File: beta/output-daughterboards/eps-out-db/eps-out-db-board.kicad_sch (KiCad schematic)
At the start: 7 parts, among them J1 EPS8 OUT FIELD, J10 TE 63951-1, J11 TE 63951-1, J12 TE 63951-1, J13 TE 63951-1, J14 TE 63951-1, J15 TE 63951-1

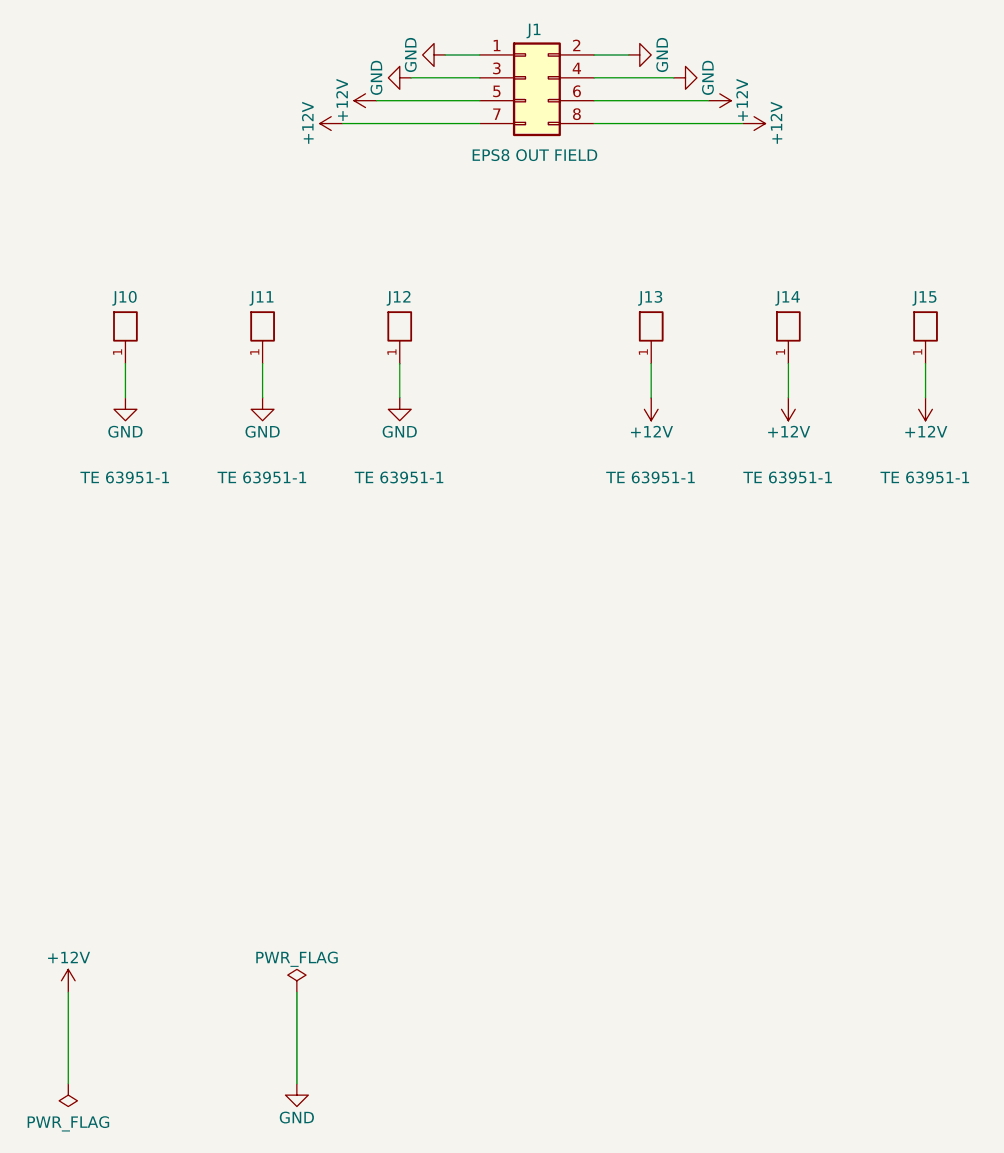
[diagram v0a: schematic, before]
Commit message: pipeline: integrate route-aware physical design flow
Generalize critical-first placement and routing, future-congestion and power-authority planning, route provenance, process watchdogs, fab/thermal validation, dashboard review, and XFCN integration. Add the supporting board contracts, component libraries, documentation, and regression coverage.
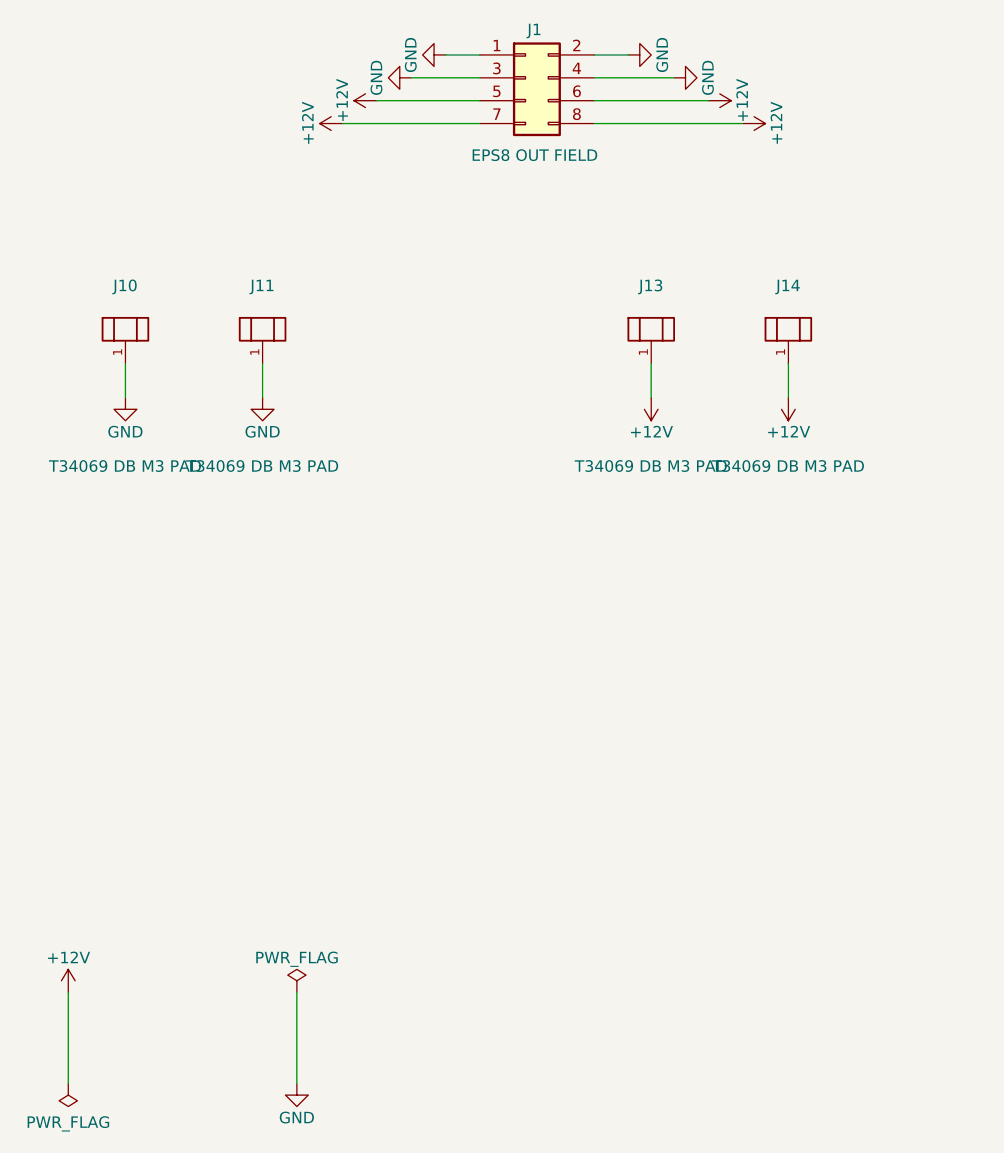
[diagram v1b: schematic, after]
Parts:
- removed J12, J15: TE 63951-1, cec-Connector_Blade:TE_63951-1_FASTON_Tab_250x032_RA_THT, symbol cec-vendor:TE_63951-1_FASTON_Tab
- J10, J11, J13, J14: value TE 63951-1 -> T34069 DB M3 PAD; footprint cec-Connector_Blade:TE_63951-1_FASTON_Tab_250x032_RA_THT -> cec-Connector_Screw:XFCN_T34069_Daughterboard_BoltPad_M3_PROVISIONAL; symbol cec-vendor:TE_63951-1_FASTON_Tab -> cec-Connector_Screw:XFCN_T34069_DB_BoltPad; Integration Note (none) -> Prototype XFCN interface; TE blade architecture remains the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; LCSC C591344 -> (none); MPN 63951-1 -> (none); Manufacturer TE Connectivity -> (none); Source Drawing (none) -> lib/datasheets/XFCN_T34069_C481452.pdf; now left out of the parts list
